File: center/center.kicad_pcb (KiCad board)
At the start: 2 copper layers, 58.2 x 64 mm, 52 parts, among them J1 top left, J2 top right, J3 bottom right, J4 bottom left, J5 SWD, Q1 AO3400, Q2 AO3401, Q3 AO3400, Q4 AO3400, Q5 AO3401, U1 AP1117-33, U2 STM32F030F4P6, Y1 8MHz

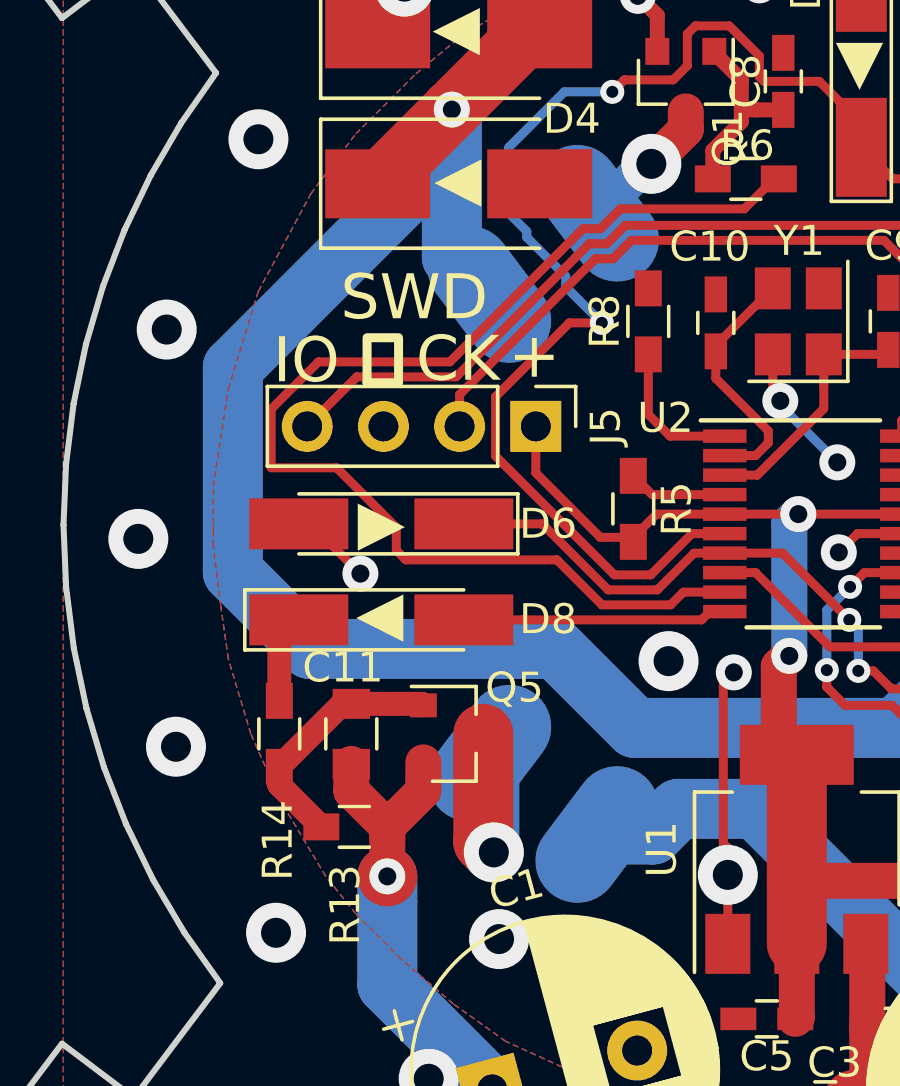
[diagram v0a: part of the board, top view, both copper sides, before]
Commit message: First AC/mux test working
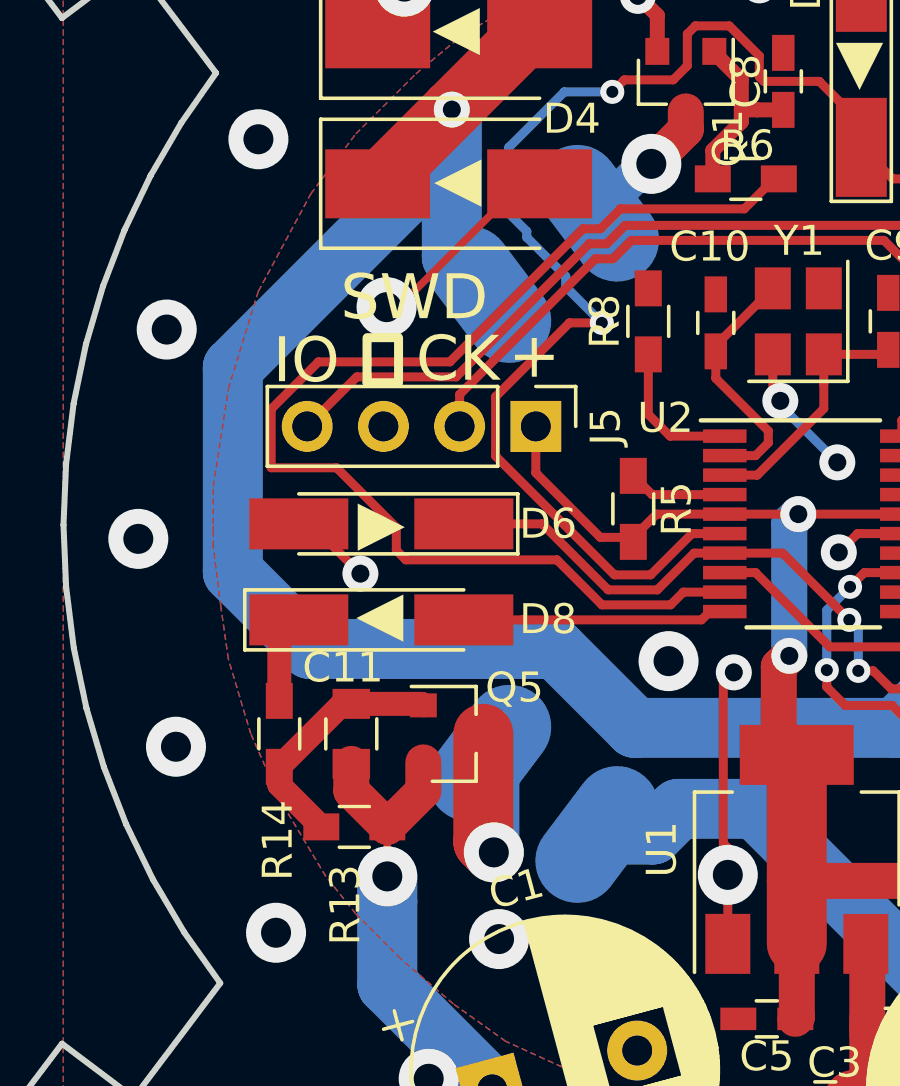
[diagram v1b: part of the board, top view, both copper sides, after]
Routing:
- net GND: track 67.0 -> 73.8 mm, vias 18 -> 19
- net +12V: vias 21 -> 22
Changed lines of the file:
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@@
     (thickness 1.6)
     (drawings 102)
-    (tracks 390)
+    (tracks 395)
     (zones 0)
     (modules 52)
@@
     (0 F.Cu signal)
     (31 B.Cu signal)
-    (32 B.Adhes user hide)
-    (33 F.Adhes user hide)
-    (34 B.Paste user hide)
-    (35 F.Paste user hide)
-    (36 B.SilkS user hide)
+    (32 B.Adhes user)
+    (33 F.Adhes user)
+    (34 B.Paste user)
+    (35 F.Paste user)
+    (36 B.SilkS user)
     (37 F.SilkS user)
-    (38 B.Mask user hide)
+    (38 B.Mask user)
     (39 F.Mask user)
     (40 Dwgs.User user)
@@
     (46 B.CrtYd user)
     (47 F.CrtYd user)
-    (48 B.Fab user hide)
+    (48 B.Fab user)
     (49 F.Fab user)
   )
@@
     (solder_mask_min_width 0.25)
     (aux_axis_origin 0 0)
-    (visible_elements FFFDFF7F)
+    (visible_elements FFFFFFFF)
     (pcbplotparams
       (layerselection 0x010fc_ffffffff)
@@
   (segment (start 84.6 108.9) (end 85.8 110.1) (width 1.2) (layer F.Cu) (net 1))
   (segment (start 84.6 108) (end 84.6 108.9) (width 1.2) (layer F.Cu) (net 1))
-  (segment (start 85.8 110.1) (end 85.8 111.75) (width 1.2) (layer F.Cu) (net 1))
   (segment (start 113.1 96.9) (end 112.95 96.75) (width 1.2) (layer F.Cu) (net 1))
   (segment (start 115.6 96.9) (end 113.1 96.9) (width 1.2) (layer F.Cu) (net 1))
@@
   (segment (start 101.35 119.2) (end 101.35 120.6) (width 2) (layer F.Cu) (net 1))
   (via (at 85.799992 111.750008) (size 1.2) (drill 0.6) (layers F.Cu B.Cu) (net 1))
-  (segment (start 85.8 111.75) (end 85.799992 111.750008) (width 2) (layer F.Cu) (net 1))
   (segment (start 89.3 118.85) (end 85.799992 115.349992) (width 2) (layer B.Cu) (net 1))
   (segment (start 85.799992 112.598536) (end 85.799992 111.750008) (width 2) (layer B.Cu) (net 1))
@@
   (via (at 106.477354 78.44672) (size 2) (drill 1) (layers F.Cu B.Cu) (net 1))
   (via (at 99.5 77.5) (size 2) (drill 1) (layers F.Cu B.Cu) (net 1))
+  (segment (start 85.8 110.1) (end 85.8 111.75) (width 0.25) (layer F.Cu) (net 1))
+  (via (at 85.799992 111.750008) (size 2) (drill 1) (layers F.Cu B.Cu) (net 1))
+  (segment (start 85.8 111.75) (end 85.799992 111.750008) (width 0.25) (layer F.Cu) (net 1))
   (via (at 95.175 104.575) (size 2) (drill 1) (layers F.Cu B.Cu) (net 2))
   (segment (start 105.5 101.025) (end 105.5 101.25) (width 0.3) (layer F.Cu) (net 2))
@@
   (segment (start 94.8 84.25) (end 94.8 83.05) (width 0.5) (layer F.Cu) (net 2))
   (segment (start 94.8 83.05) (end 94.15 82.4) (width 0.5) (layer F.Cu) (net 2))
+  (via (at 85.775634 92.775634) (size 2) (drill 1) (layers F.Cu B.Cu) (net 2))
+  (segment (start 86.16539 92.775634) (end 85.775634 92.775634) (width 0.25) (layer F.Cu) (net 2))
+  (segment (start 90.878544 88.66248) (end 90.278544 88.66248) (width 0.25) (layer F.Cu) (net 2))
+  (segment (start 90.278544 88.66248) (end 86.16539 92.775634) (width 0.25) (layer F.Cu) (net 2))
   (segment (start 94.775 99.675) (end 94 100.45) (width 0.3) (layer F.Cu) (net 3))
   (segment (start 97.05 99.675) (end 94.775 99.675) (width 0.3) (layer F.Cu) (net 3))

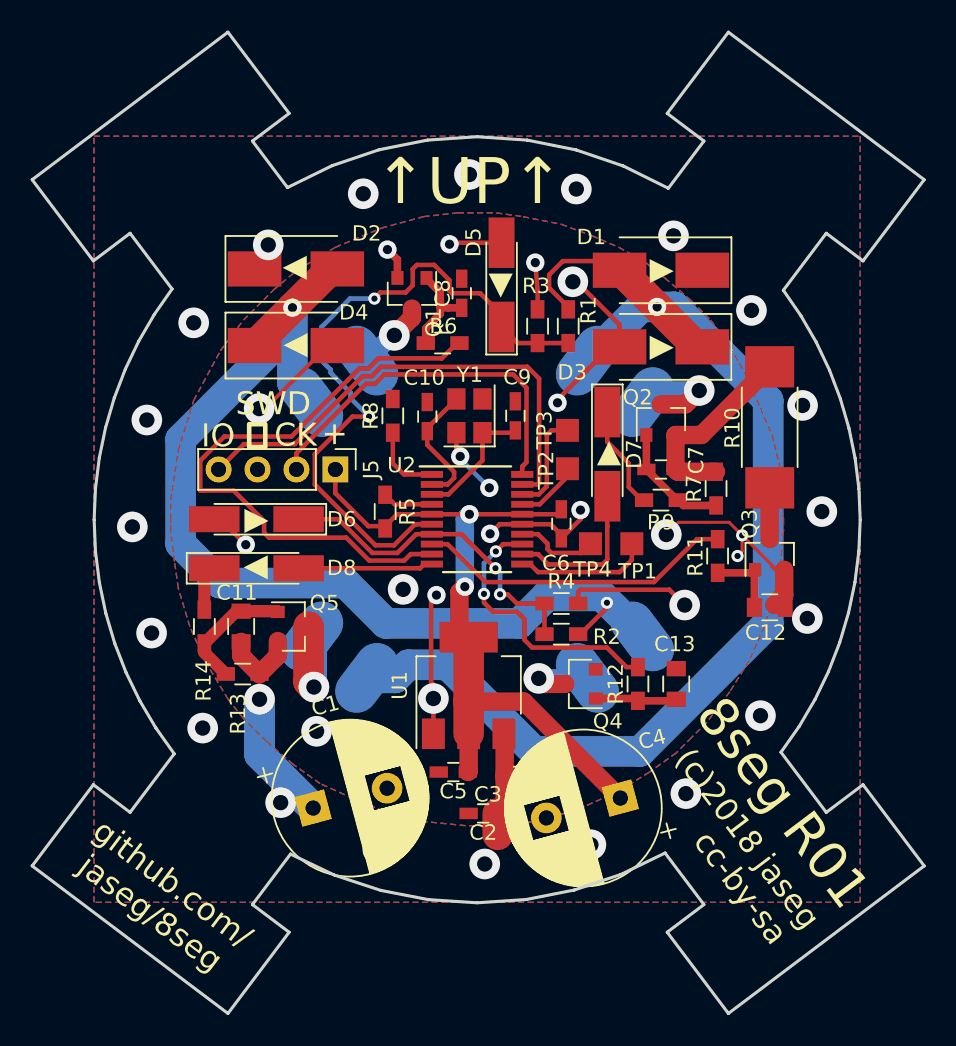
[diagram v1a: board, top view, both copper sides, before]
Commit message: center: fix tape footprint polarity, vcc short, silk
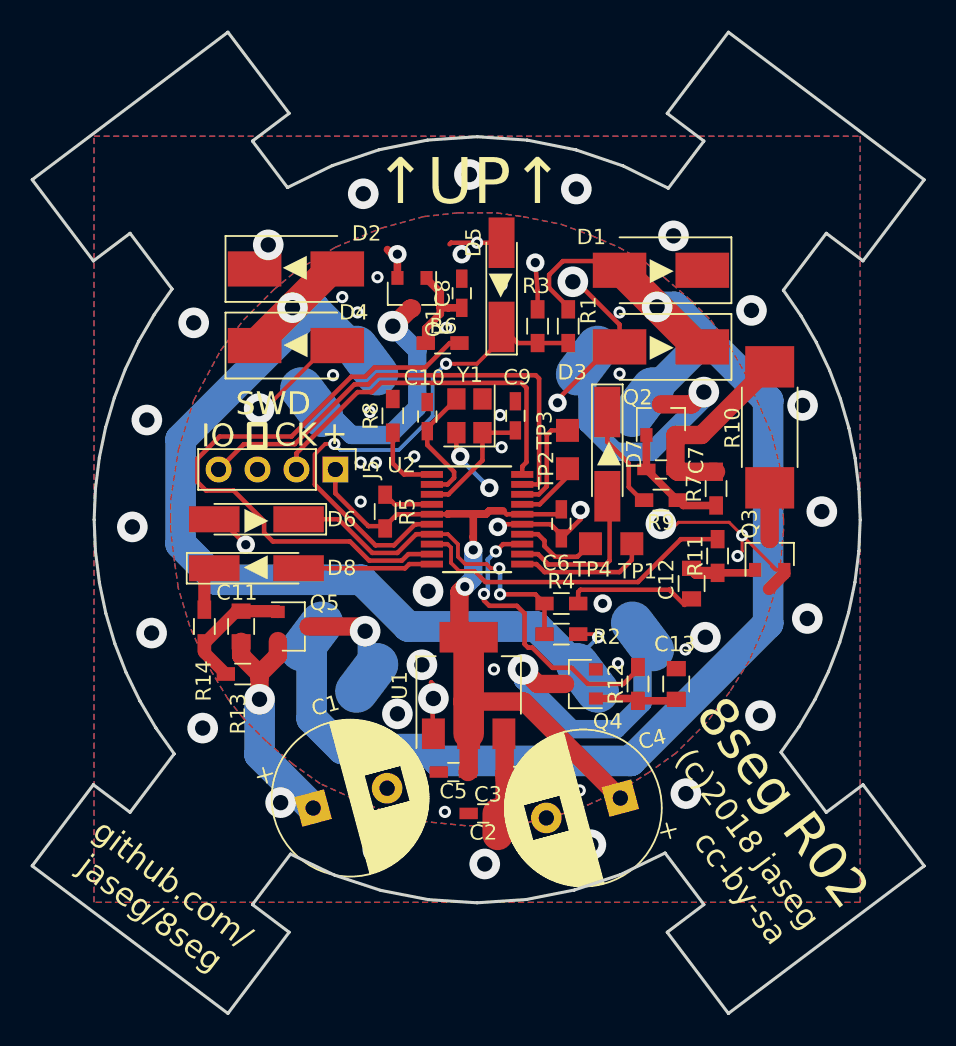
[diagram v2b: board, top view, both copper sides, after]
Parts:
- moved C12 5.33 mm to (114.0, 104.2), turned to 270 degrees
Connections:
- J1 pad 1: Net-(D1-Pad2) -> /Q2
- J1 pad 2: /Q2 -> Net-(D1-Pad2)
- J2 pad 1: Net-(D2-Pad2) -> /Q0
- J2 pad 2: /Q0 -> Net-(D2-Pad2)
- J3 pad 1: Net-(D1-Pad2) -> /Q3
- J3 pad 2: /Q3 -> Net-(D1-Pad2)
- J4 pad 1: Net-(D2-Pad2) -> /Q1
- J4 pad 2: /Q1 -> Net-(D2-Pad2)
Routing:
- net /Q1: track 5.07 -> 18.0 mm
- net /Q2: track 6.89 -> 17.5 mm
- net /Vmeas_A: track 44.9 -> 34.5 mm
- net /Q0: track 4.99 -> 14.3 mm
- net Net-(D1-Pad2): track 78.1 -> 85.8 mm
- net GND: track 73.8 -> 67.7 mm, vias 19 -> 42
- net +3V3: track 47.7 -> 49.4 mm
- net /CH1: track 18.2 -> 19.5 mm
- net Net-(D2-Pad2): track 68.5 -> 67.6 mm
- net /Vmeas_B: track 22.2 -> 22.8 mm
- net /LOAD: track 20.8 -> 21.4 mm
- net Net-(C12-Pad1): track 5.00 -> 4.43 mm
- net /Q3: track 7.46 -> 6.91 mm
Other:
- board text added: "8seg R02"
- board text removed: "8seg R01"
